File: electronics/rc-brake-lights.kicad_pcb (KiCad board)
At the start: 2 copper layers, 22 x 10 mm, 8 parts, among them J1 TH, J2 LED, U1 STC15x10x

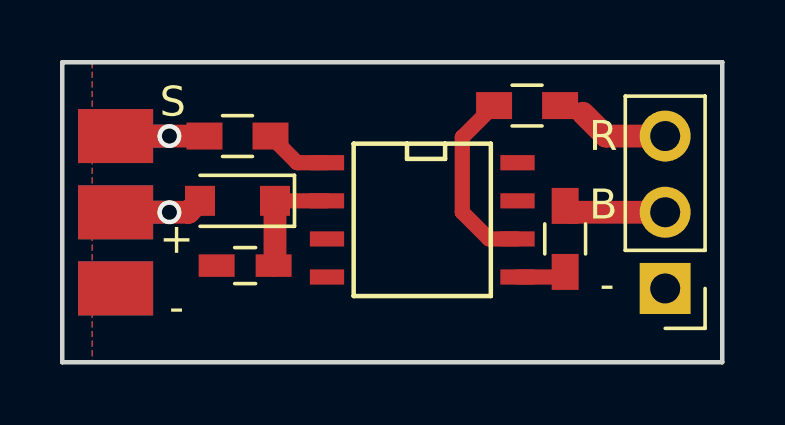
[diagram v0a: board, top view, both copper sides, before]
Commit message: Move IO pins so we can use T0 to measure pulse width
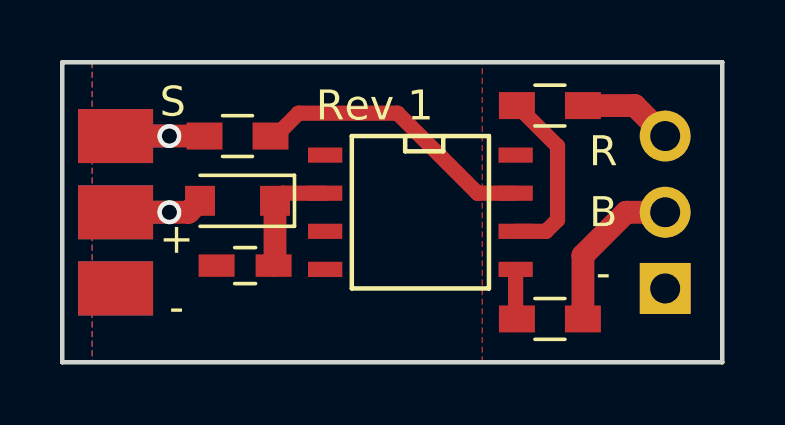
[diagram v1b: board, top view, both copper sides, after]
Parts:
- D1: value D -> 1N4148
- U1: value STC15x10x -> STC15W104
- moved R3 2.71 mm to (116.3, 103.6), turned to 180 degrees
- moved R2 0.76 mm to (116.3, 96.4)
- moved U1 0.26 mm to (111.9, 100.0)
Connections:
- U1 pad 1: /TH_R -> (no net)
- U1 pad 7: (no net) -> /TH_R
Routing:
- net /TH_R: track 2.25 -> 9.59 mm
- net /Brake_LED: track 3.42 -> 5.45 mm
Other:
- board text added: "Rev 1"

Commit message: Add setup button
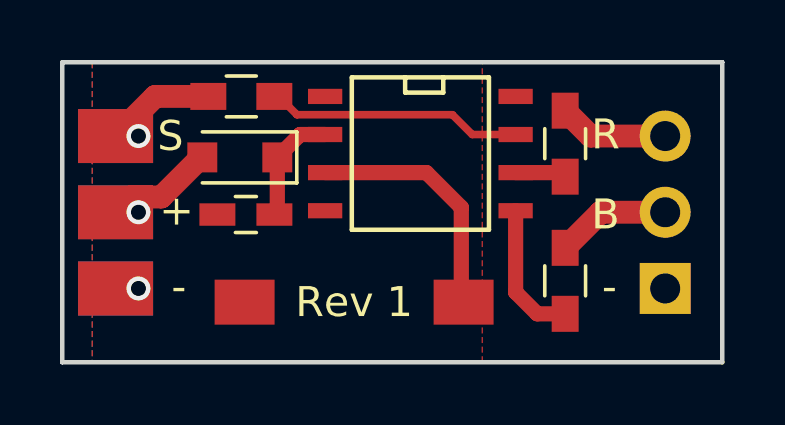
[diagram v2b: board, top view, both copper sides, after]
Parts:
- added SW1: Setup button, WLA:Tact_switch_SMD_6x3_6x2_5, F.Cu at (109.7, 103.0)
- moved U1 1.96 mm to (111.9, 98.0)
- moved C1 1.70 mm to (106.1, 100.1)
- moved D1 1.45 mm to (105.9, 98.2)
- moved R2 1.37 mm to (116.8, 97.7), turned to 270 degrees
- moved R3 1.37 mm to (116.8, 102.3), turned to 270 degrees
- moved R1 1.33 mm to (106.0, 96.1)
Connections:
- U1 pad 3: (no net) -> Net-(SW1-Pad2)
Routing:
- net Net-(SW1-Pad2): track 0.00 -> 8.18 mm
- net /Reverse: track 5.93 -> 1.71 mm
- net /Brake: track 1.67 -> 4.67 mm
- net /Brake_LED: track 5.45 -> 3.83 mm
- net /TH_R: track 9.59 -> 8.57 mm
- net GND: track 0.00 -> 0.76 mm, vias 0 -> 1
- net /Reverse_LED: track 3.16 -> 3.68 mm
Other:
- rule pad_to_mask_clearance: 0.2032 -> 0.1524
